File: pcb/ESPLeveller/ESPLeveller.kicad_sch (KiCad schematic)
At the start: 12 parts, among them J1 Battery_18650x2, J2 Sensor_Pod, J3 OPT_BTN, SW1 PWR, U1 ESP32C3_SuperMini, U2 TP4056_ChargeProt, U3 MT3608_5V

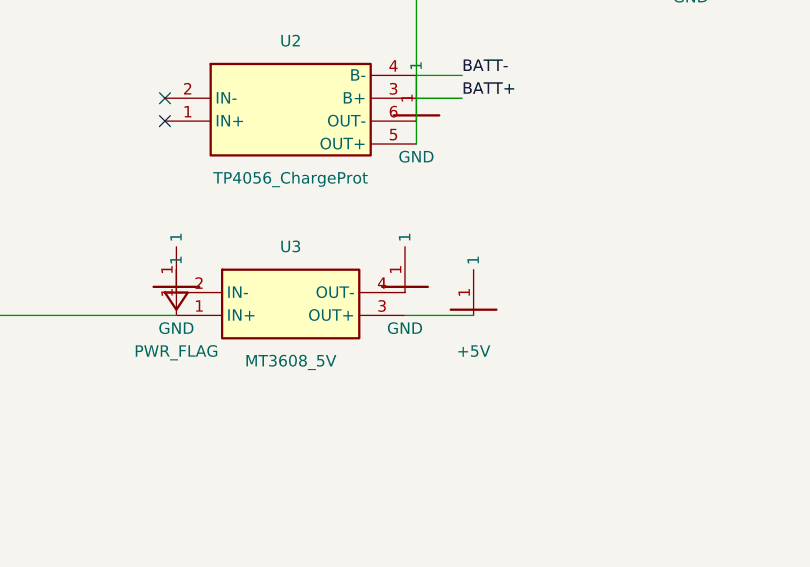
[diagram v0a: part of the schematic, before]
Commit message: feat(pcb): P2 layout — routed, poured, DRC-clean
105x75mm 2-layer carrier. Placement signal-flow (TP4056->SW->MT3608->
SuperMini), Freerouting 2.1.0 + Temurin 21 (29 traces, 0 incomplete,
0 clearance violations), GND pour on B.Cu with solid pad connections.
ERC 0 errors after OUT- pins -> passive + PWR_FLAG on GND. Netlist
re-exported and verified identical to P1. Remaining: 4 silk warnings
(intra-footprint module labels, cosmetic) + footprint-field parity
noise. Reproducible pipeline scripts (p2_*.py).
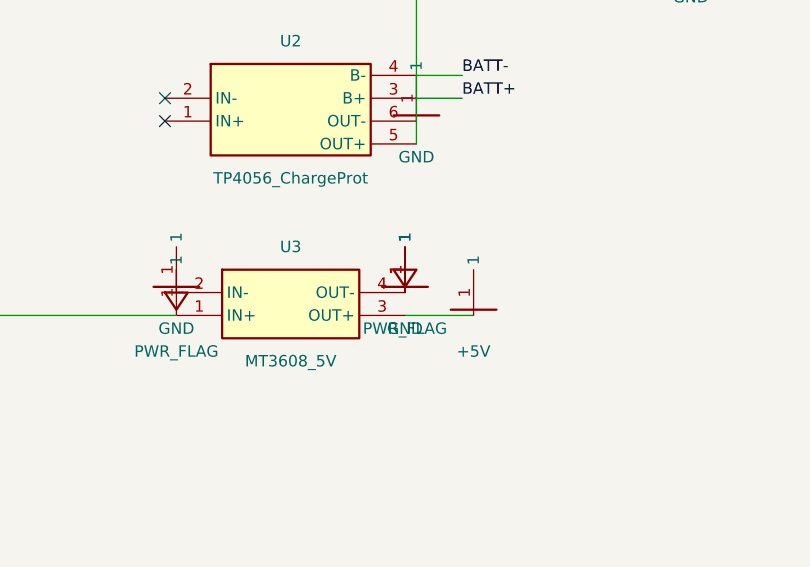
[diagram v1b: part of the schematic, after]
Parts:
- SW1: footprint Button_Switch_THT:SW_SPST_PTS645_V -> Button_Switch_THT:SW_Tactile_SPST_Angled_PTS645Vx31-2LFS
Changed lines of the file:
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@@
       (property "Reference" "SW1" (at 81.28 44.45 0) (effects (font (size 1.27 1.27))))
       (property "Value" "PWR" (at 81.28 59.69 0) (effects (font (size 1.27 1.27))))
-      (property "Footprint" "Button_Switch_THT:SW_SPST_PTS645_V" (at 81.28 52.07 0) (effects (font (size 1.27 1.27)) (hide yes)))
+      (property "Footprint" "Button_Switch_THT:SW_Tactile_SPST_Angled_PTS645Vx31-2LFS" (at 81.28 52.07 0) (effects (font (size 1.27 1.27)) (hide yes)))
       (property "Datasheet" "~" (at 81.28 52.07 0) (effects (font (size 1.27 1.27)) (hide yes)))
       (property "Description" "SW_Push" (at 81.28 52.07 0) (effects (font (size 1.27 1.27)) (hide yes)))
@@
     (no_connect (at 212.01 67.31))
     (no_connect (at 212.01 69.85))
-    (symbol
+        (symbol
+      (lib_id "PWR_FLAG")
+      (at 128.27 93.98 0)
+      (unit 1)
+      (exclude_from_sim no) (in_bom no) (on_board yes) (dnp no)
+      (property "Reference" "#FLG02" (at 128.27 96.48 0) (effects (font (size 1.27 1.27)) (hide yes)))
+      (property "Value" "PWR_FLAG" (at 128.27 97.98 0) (effects (font (size 1.27 1.27))))
+      (property "Footprint" "" (at 128.27 93.98 0) (effects (font (size 1.27 1.27)) (hide yes)))
+      (property "Datasheet" "~" (at 128.27 93.98 0) (effects (font (size 1.27 1.27)) (hide yes)))
+      (property "Description" "power symbol" (at 128.27 93.98 0) (effects (font (size 1.27 1.27)) (hide yes)))
+      (pin "1")
+      (instances
+        (project "ESPLeveller"
+          (path "/a9a0ded6-8392-467b-8613-40d4fc2ddccc"
+            (reference "#FLG02") (unit 1)
+          )
+        )
+      )
+    )
+(symbol
       (lib_id "PWR_FLAG")
       (at 102.87 96.52 0)
@@
       )
     )
-    (sheet_instances
+    	(wire (pts (xy 129.54 77.47) (xy 129.54 77.47))
+	)
+(sheet_instances
       (path "/" (page "1"))
     )
